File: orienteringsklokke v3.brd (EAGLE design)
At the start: 40.8 x 50 mm, 16 parts

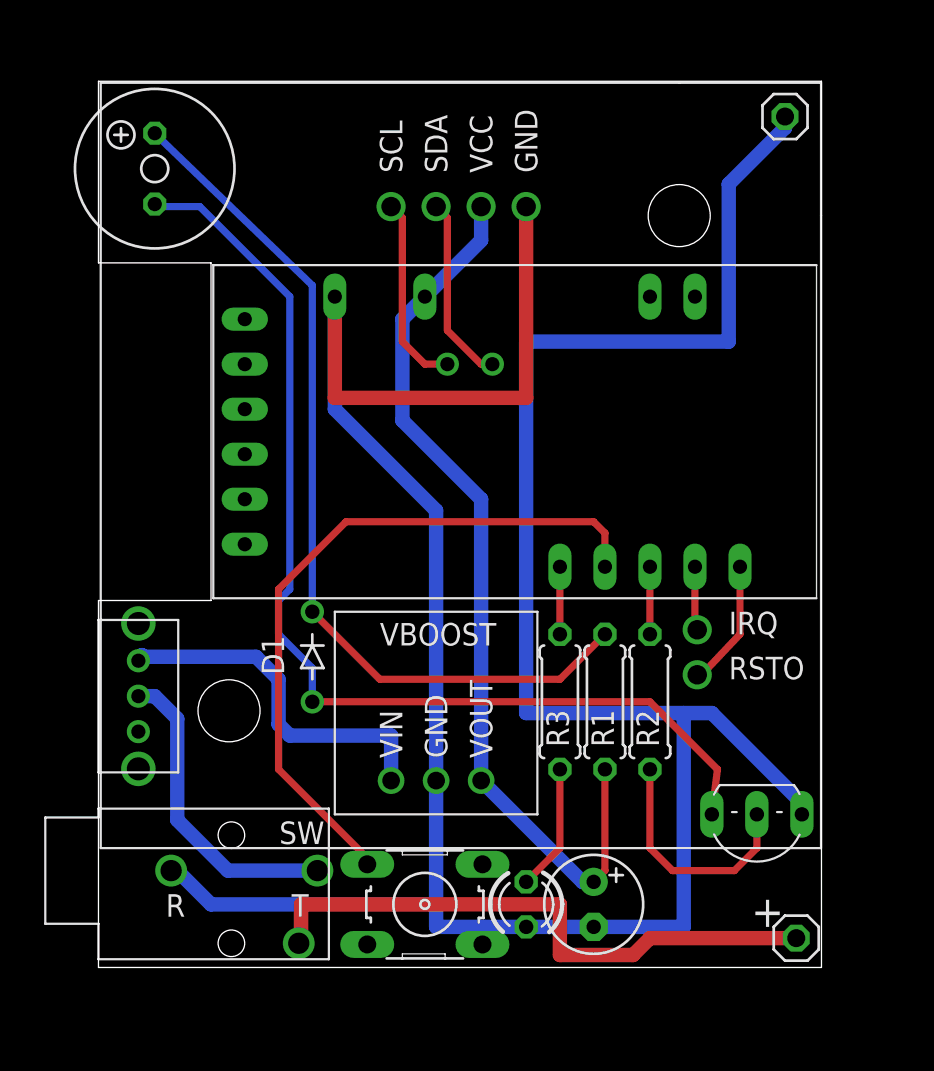
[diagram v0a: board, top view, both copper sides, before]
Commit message: Rotated battery 90 degrees, working on case layout
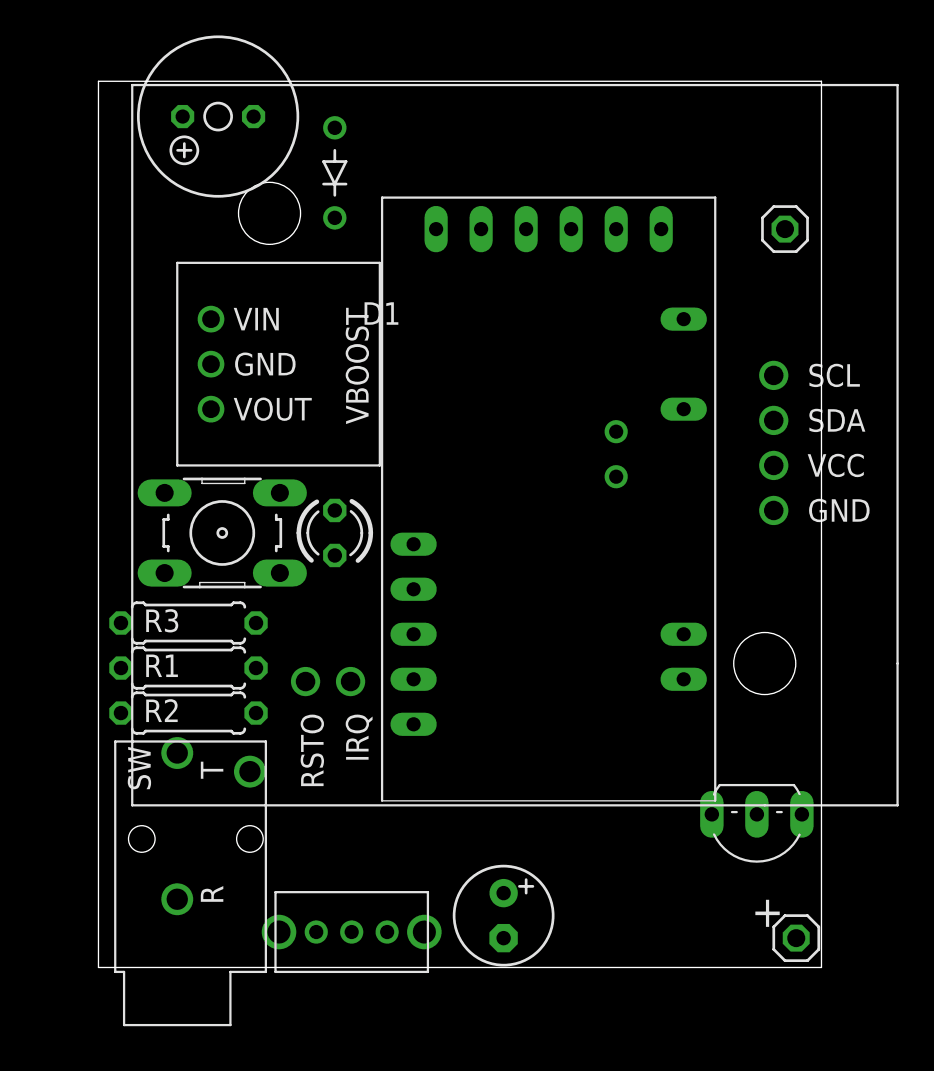
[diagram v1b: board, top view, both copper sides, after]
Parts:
- moved D1 27.3 mm to (13.3, 45.1), turned to 90 degrees
- moved U$3 26.7 mm to (6.35, 34.3), turned to 270 degrees
- moved R2 26.0 mm to (5.08, 14.6), turned to 180 degrees
- moved S1 23.9 mm to (6.99, 24.8), turned to 180 degrees
- moved LED1 23.6 mm to (13.3, 24.8)
- moved R1 23.6 mm to (5.08, 17.1), turned to 0 degrees
- moved U$2 22.1 mm to (38.1, 26.0), turned to 180 degrees
- moved R3 21.4 mm to (5.08, 19.7), turned to 180 degrees
- moved U$6 21.1 mm to (14.3, 0.00), turned to 180 degrees
- moved CHARGE 7.24 mm to (4.45, 0.00), turned to 90 degrees
- moved BATTERY_GND 6.35 mm to (38.7, 41.9)
- moved C1 5.12 mm to (22.9, 3.17)
- moved U$1 4.63 mm to (6.75, 48.3), turned to 180 degrees
- moved U$4 4.26 mm to (25.4, 26.7), turned to 0 degrees
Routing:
- net GND: track 172.7 -> 0.00 mm
- net N$2: track 60.7 -> 0.00 mm
- net +3V3: track 51.4 -> 0.00 mm
- net N$4: track 49.9 -> 0.00 mm
- net SWITCH: track 39.8 -> 0.00 mm
- net N$6: track 33.9 -> 0.00 mm
- net N$7: track 20.3 -> 0.00 mm
- net N$1: track 17.5 -> 0.00 mm
- net N$3: track 13.4 -> 0.00 mm
- net SCL: track 10.9 -> 0.00 mm
- net SDA: track 10.6 -> 0.00 mm
- net RSTO: track 7.21 -> 0.00 mm
- net N$5: track 7.14 -> 0.00 mm
- net LED: track 3.81 -> 0.00 mm
- net BUZZER: track 3.81 -> 0.00 mm
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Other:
- outline, holes or cut-outs redrawn

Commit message: Lots of work on version 3
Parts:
- removed S1: (no value), switch-omron:B3F-10XX
- added LED2: (no value), led:LED3MM
- added R4: 220, resistor:0204/5
- added U$5: PUSHBUTTON_2P, joakim:PUSHBUTTON_HORIZ_J
- C1: device resistor:E2,5-6 -> joakim:CAP-HORIZ-6.5X11X2.5
- R1, R2, R3: device resistor:0207/7 -> resistor:0204/5
- U$1: value BUZZER_J -> BUZZER_JL; device joakim:BUZZER_J -> joakim:BUZZER_HORIZ_J_LEFT
- U$2: value NFC_MODULE_V3_I2C -> NFC_MODULE_V3_I2CC; device joakim:NFC_MODULE_V3_I2C -> joakim:NFC_MODULE_V3_I2C_CENTERED
- moved T1 37.8 mm to (12.1, 35.9), turned to 90 degrees
- moved C1 35.8 mm to (5.08, 34.3), turned to 90 degrees
- moved R2 28.4 mm to (10.2, 42.5), turned to 270 degrees
- moved U$1 25.0 mm to (-3.49, 25.4), turned to 90 degrees
- moved D1 17.7 mm to (6.99, 28.6), turned to 0 degrees
- moved U$3 14.7 mm to (5.08, 19.7)
- moved U$2 14.6 mm to (23.5, 25.4), turned to 90 degrees
- moved LED1 13.7 mm to (1.91, 17.1)
- moved R1 13.5 mm to (6.99, 30.5), turned to 180 degrees
- moved R3 7.24 mm to (6.99, 26.7)
- moved BATTERY_VCC 4.45 mm to (34.9, 1.91)
- moved BATTERY_GND 4.26 mm to (34.9, 43.8)
- moved U$4 3.42 mm to (24.1, 29.8)
- moved CHARGE 0.64 mm to (3.81, 0.00)
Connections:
- net LED renamed LED1
- new net LED2: R4.1
- new net N$8: LED2.A, R4.2
- net GND: now also LED2.K, U$5.2; no longer S1.4
- net SWITCH: now also U$5.1; no longer S1.1
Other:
- board size 40.8 x 50 mm -> 36.8 x 50.2 mm
- board text added: "Husk overgang mellom side og batterikontakt"

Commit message: Hopefully final layout, tracing left
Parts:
- BATTERY_GND, BATTERY_VCC: value (none) -> DUPONT-PIN-90DEG; device joakim:MA01-1J -> joakim:DUPONT-PIN-90DEG
- R1: value 100 -> 68
- U$2: value NFC_MODULE_V3_I2CC -> NFC_MODULE_V3_SPI; device joakim:NFC_MODULE_V3_I2C_CENTERED -> joakim:NFC_MODULE_V3_SPI_CENTERED
- U$5: value PUSHBUTTON_2P -> PUSHBUTTON_2P6MM; device joakim:PUSHBUTTON_HORIZ_J -> joakim:PUSHBUTTON_HORIZ_6MM_J
- moved BATTERY_VCC 16.5 mm to (34.9, 18.4)
- moved BATTERY_GND 15.2 mm to (34.9, 28.6), turned to 180 degrees
- moved R2 10.5 mm to (12.7, 32.4), turned to 90 degrees
- moved U$3 7.65 mm to (12.7, 19.1), turned to 90 degrees
- moved T1 4.72 mm to (10.5, 40.3)
- moved LED2 1.91 mm to (1.91, 31.8)
- moved LED1 1.90 mm to (1.91, 15.2)
- moved U$1 1.90 mm to (-3.49, 23.5)
- moved U$2 1.90 mm to (23.5, 23.5), turned to 180 degrees
- moved R1 0.64 mm to (6.99, 29.8)
- moved R3 0.64 mm to (6.99, 26.0)
- moved CHARGE 0.64 mm to (4.45, 0.00)
- moved U$6 0.63 mm to (14.9, 0.00)
- moved C1 0.63 mm to (5.08, 33.7)
- moved D1 0.63 mm to (6.99, 27.9)
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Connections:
- removed net IRQ: U$2.IRQ, U$4.D7
- removed net RSTO: U$2.RSTO, U$4.D8
- new net MISO: U$2.MISO, U$4.D12
- new net MOSI: U$2.MOSI, U$4.D11
- new net SCK: U$2.SCK, U$4.D13
- new net SS: U$2.SS, U$4.D10
- net BUZZER: now also U$4.D3; no longer U$4.D6
- net LED2: now also U$4.D2
- net SCL: no longer U$2.SCL
- net SDA: no longer U$2.SDA
- net SWITCH: now also U$4.D8; no longer U$4.D5
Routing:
- net GND: track 0.00 -> 113.3 mm
- net SS: track 0.00 -> 12.6 mm
- net N$4: track 0.00 -> 6.16 mm
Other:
- board size 36.8 x 50.2 mm -> 36.2 x 47 mm
- board text removed: "Husk overgang mellom side og batterikontakt"

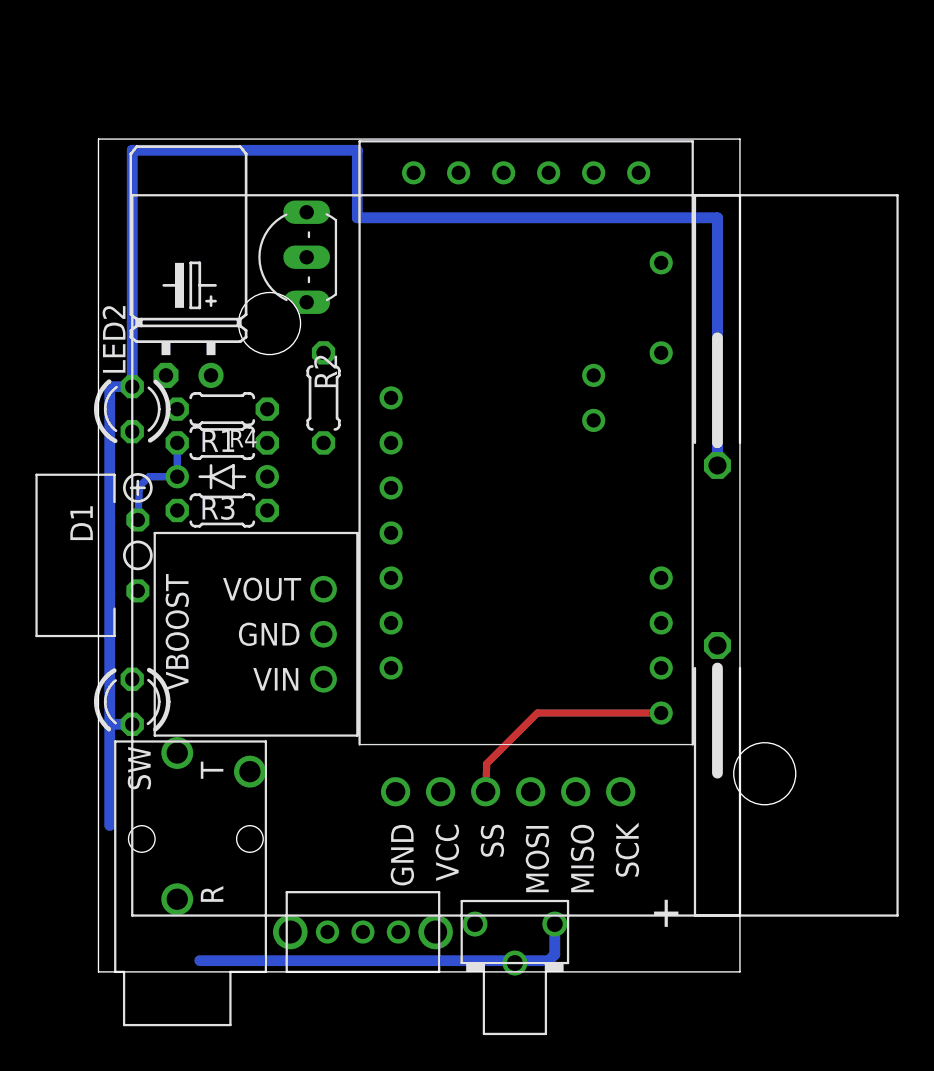
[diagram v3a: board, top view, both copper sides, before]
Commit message: Traced and fixed most silk screening
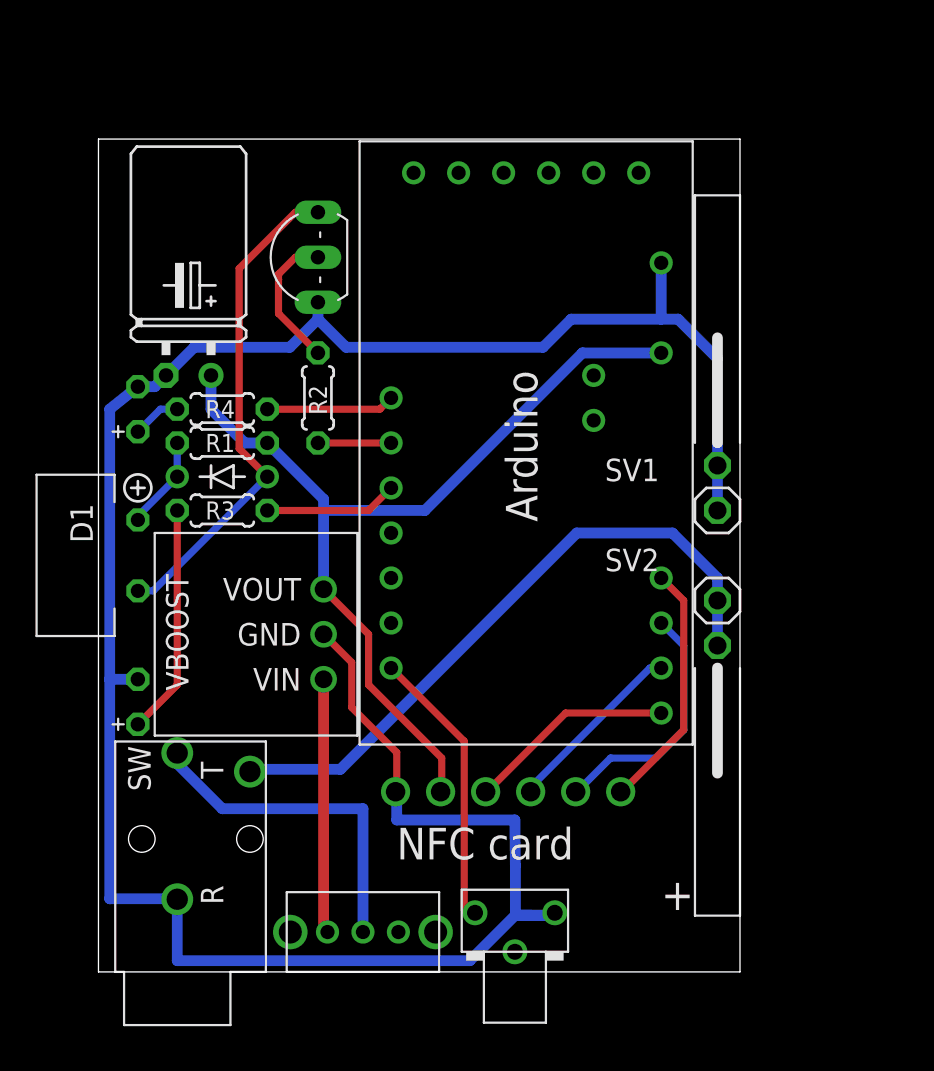
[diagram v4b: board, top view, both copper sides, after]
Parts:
- added SV1, SV2: (no value), joakim:MA01-1J
- LED1, LED2: device led:LED3MM -> joakim:LED90DEG_LEFT
- U$2: value NFC_MODULE_V3_SPI -> NFC_MODULE_V3_SPINH; device joakim:NFC_MODULE_V3_SPI_CENTERED -> joakim:NFC_MODULE_V3_SPI_CENTERED_NO_HOLES
- moved T1 0.64 mm to (11.1, 40.3)
- moved U$5 0.64 mm to (23.5, 0.64)
- moved LED1 0.32 mm to (2.22, 15.2), turned to 90 degrees
- moved LED2 0.32 mm to (2.22, 31.8)
- moved R2 0.32 mm to (12.4, 32.4)
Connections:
- net GND: now also SV1.1
- net N$6: now also SV2.1
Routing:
- net +3V3: track 0.00 -> 52.4 mm
- net N$6: track 0.00 -> 36.8 mm
- net N$2: track 0.00 -> 28.1 mm
- net GND: track 113.3 -> 136.8 mm
- net N$1: track 0.00 -> 19.2 mm
- net SWITCH: track 0.00 -> 16.7 mm
- net N$7: track 0.00 -> 14.4 mm
- net SCK: track 0.00 -> 14.1 mm
- net MISO: track 0.00 -> 14.1 mm
- net N$5: track 0.00 -> 13.0 mm
- net MOSI: track 0.00 -> 10.4 mm
- net N$3: track 0.00 -> 7.98 mm
- net LED1: track 0.00 -> 7.51 mm
- net LED2: track 0.00 -> 7.25 mm
- net BUZZER: track 0.00 -> 4.13 mm
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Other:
- board text added: "Arduino"
- board text added: "NFC card"
